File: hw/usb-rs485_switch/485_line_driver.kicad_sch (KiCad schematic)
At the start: 26 parts, among them Q15 Q_NPN_BEC, Q16 Si2301CDS, U26 INA180A2, U27 MAX485E

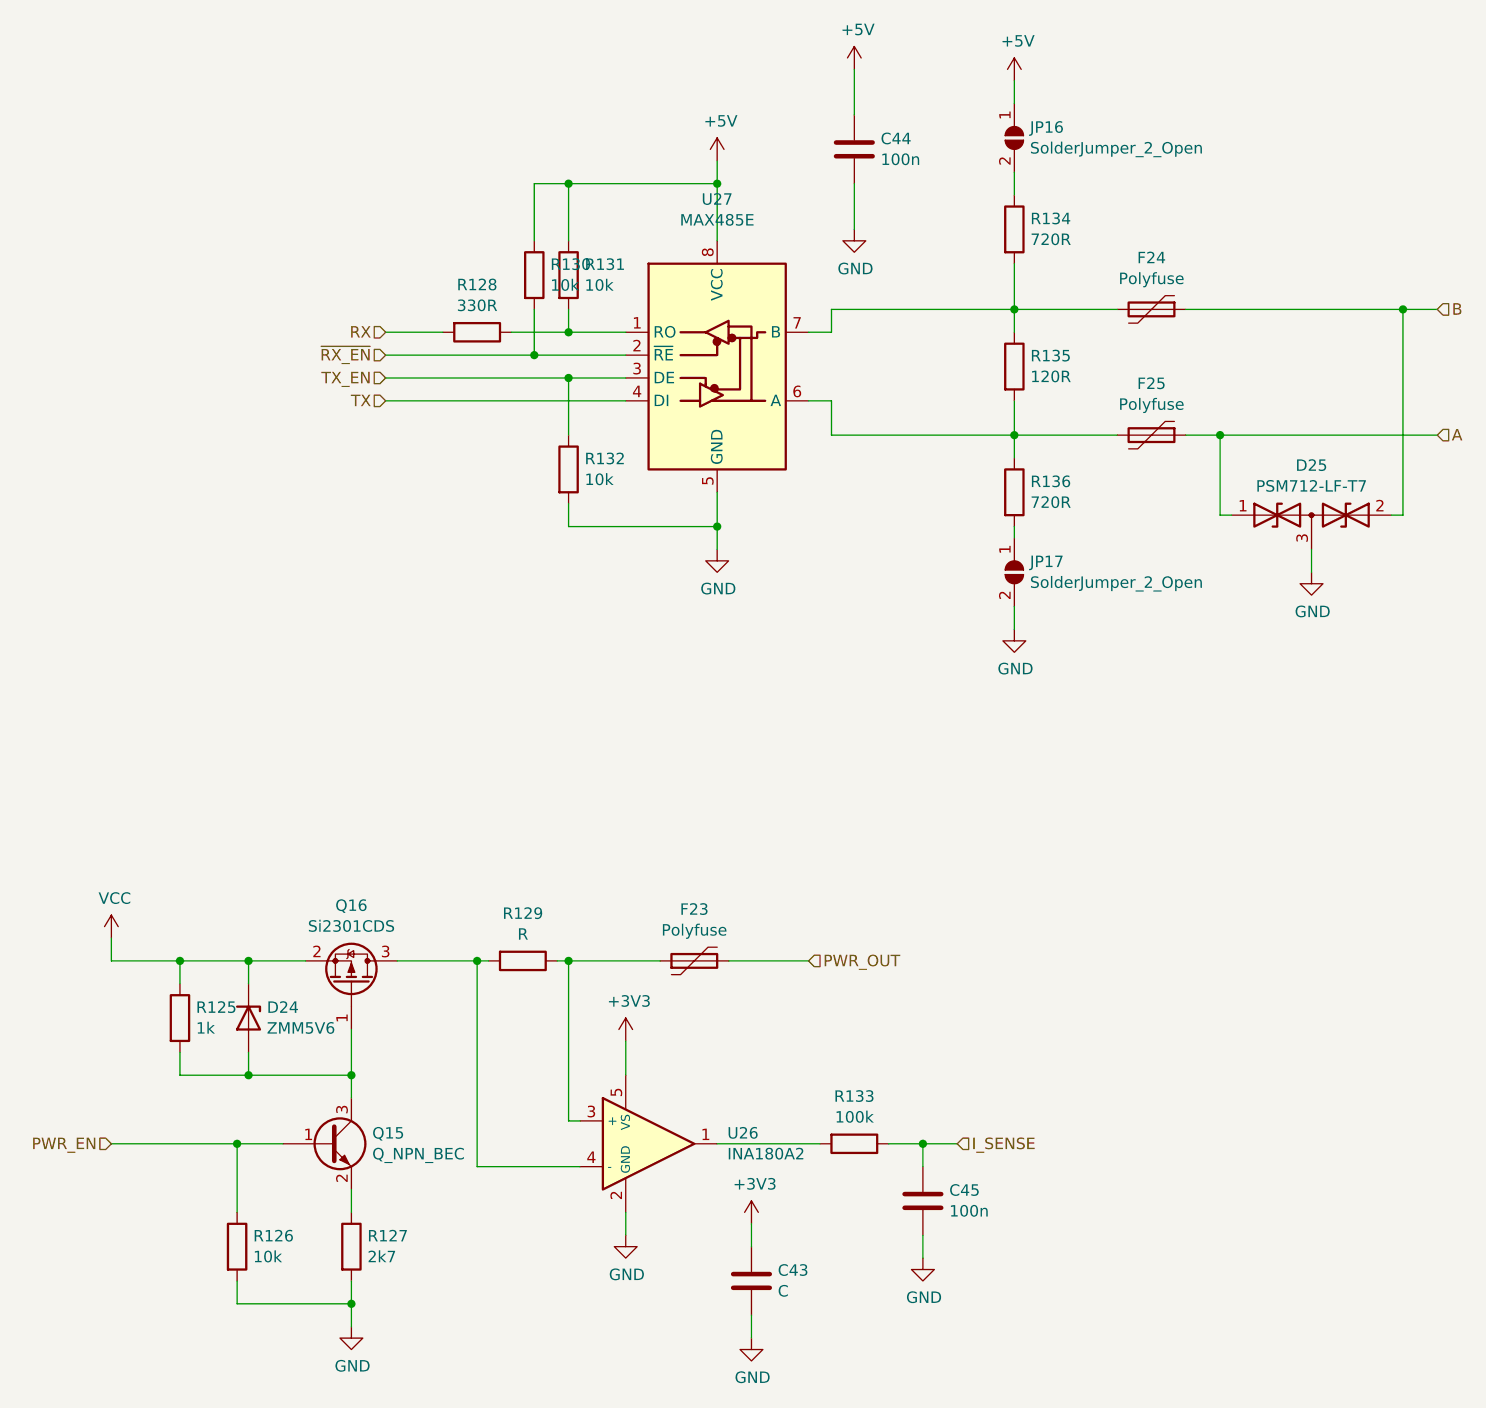
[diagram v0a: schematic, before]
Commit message: Assigned footprints, started routing.
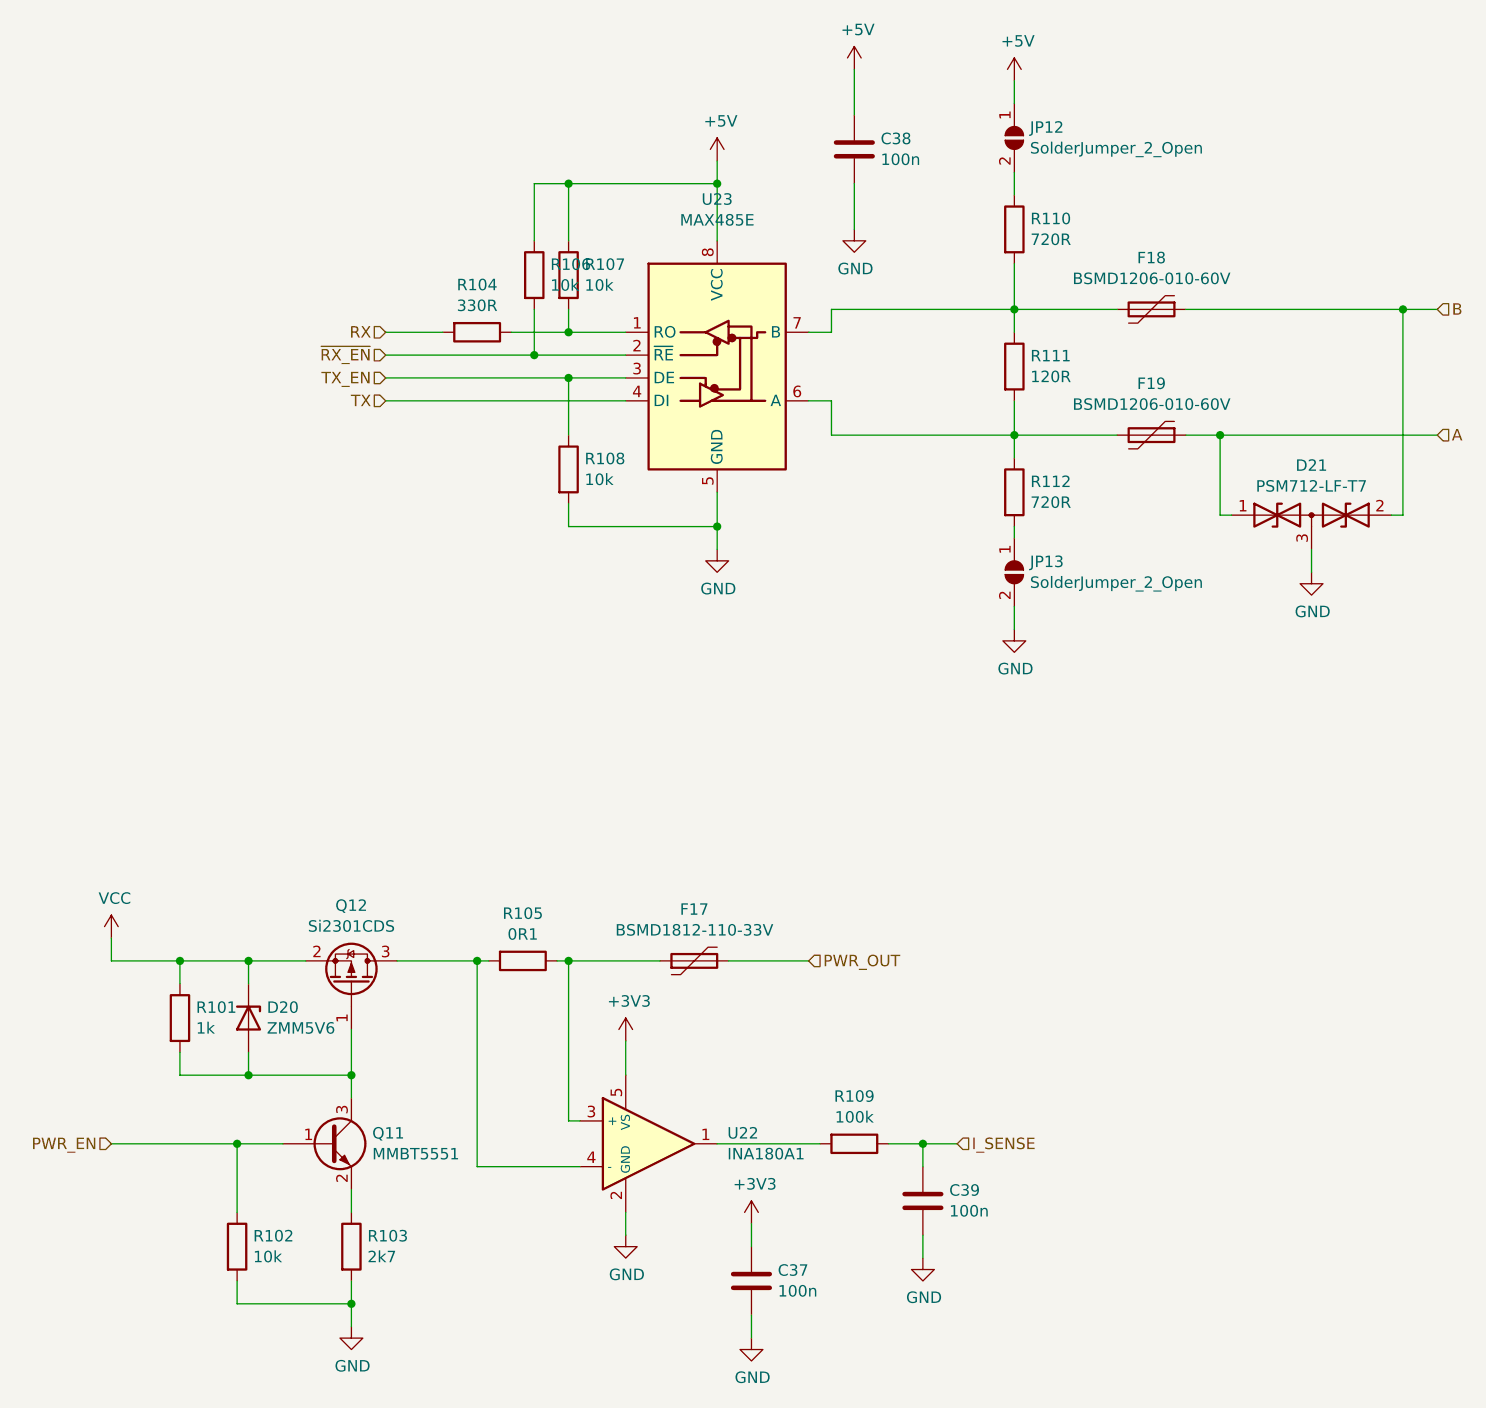
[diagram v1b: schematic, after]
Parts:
- C37: renamed from C43; value C -> 100n; footprint (none) -> Capacitor_SMD:C_0603_1608Metric
- C38: renamed from C44; footprint (none) -> Capacitor_SMD:C_0603_1608Metric
- C39: renamed from C45; footprint (none) -> Capacitor_SMD:C_0603_1608Metric
- D21: renamed from D25; footprint (none) -> Package_TO_SOT_SMD:SOT-23
- F17: renamed from F23; value Polyfuse -> BSMD1812-110-33V; footprint (none) -> Fuse:Fuse_1812_4532Metric; LCSC (none) -> C883150
- F18: renamed from F24; value Polyfuse -> BSMD1206-010-60V; footprint (none) -> Fuse:Fuse_1206_3216Metric; LCSC (none) -> C883116
- F19: renamed from F25; value Polyfuse -> BSMD1206-010-60V; footprint (none) -> Fuse:Fuse_1206_3216Metric; LCSC (none) -> C883116
- JP12: renamed from JP16; footprint (none) -> Jumper:SolderJumper-2_P1.3mm_Open_TrianglePad1.0x1.5mm
- JP13: renamed from JP17; footprint (none) -> Jumper:SolderJumper-2_P1.3mm_Open_TrianglePad1.0x1.5mm
- Q11: renamed from Q15; value Q_NPN_BEC -> MMBT5551; footprint (none) -> Package_TO_SOT_SMD:SOT-23; LCSC (none) -> C2145
- R101: renamed from R125; footprint (none) -> Resistor_SMD:R_0603_1608Metric
- R102: renamed from R126; footprint (none) -> Resistor_SMD:R_0603_1608Metric
- R103: renamed from R127; footprint (none) -> Resistor_SMD:R_0603_1608Metric
- R104: renamed from R128; footprint (none) -> Resistor_SMD:R_0603_1608Metric
- R105: renamed from R129; value R -> 0R1; footprint (none) -> Resistor_SMD:R_1206_3216Metric; LCSC (none) -> C25334
- R106: renamed from R130; footprint (none) -> Resistor_SMD:R_0603_1608Metric
- R107: renamed from R131; footprint (none) -> Resistor_SMD:R_0603_1608Metric
- R108: renamed from R132; footprint (none) -> Resistor_SMD:R_0603_1608Metric
- R109: renamed from R133; footprint (none) -> Resistor_SMD:R_0603_1608Metric
- R110: renamed from R134; footprint (none) -> Resistor_SMD:R_0603_1608Metric
- R111: renamed from R135; footprint (none) -> Resistor_SMD:R_0603_1608Metric
- R112: renamed from R136; footprint (none) -> Resistor_SMD:R_0603_1608Metric
- U22: renamed from U26; value INA180A2 -> INA180A1; footprint (none) -> Package_TO_SOT_SMD:SOT-23-5; LCSC (none) -> C122228
- U23: renamed from U27; footprint (none) -> Package_SO:SOIC-8_3.9x4.9mm_P1.27mm
- renumbered D24 to D20, Q16 to Q12

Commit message: Routing in progress.
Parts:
- renumbered C37 to C31, C38 to C32, C39 to C33, D20 to D16, D21 to D17, F17 to F11, F18 to F12, F19 to F13, JP12 to JP8, JP13 to JP9, Q11 to Q7, Q12 to Q8, R101 to R77, R102 to R78, R103 to R79, R104 to R80, R105 to R81, R106 to R82, R107 to R83, R108 to R84, R109 to R85, R110 to R86, R111 to R87, R112 to R88, U22 to U18, U23 to U19

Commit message: Routing in progress...
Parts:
- renumbered C31 to C25, C32 to C26, C33 to C27, D16 to D12, D17 to D13, F11 to F5, F12 to F6, F13 to F7, JP8 to JP4, JP9 to JP5, Q7 to Q3, Q8 to Q4, R77 to R53, R78 to R54, R79 to R55, R80 to R56, R81 to R57, R82 to R58, R83 to R59, R84 to R60, R85 to R61, R86 to R62, R87 to R63, R88 to R64, U18 to U14, U19 to U15

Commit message: Routed.
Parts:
- renumbered C25 to C22, C26 to C23, C27 to C24, D12 to D10, D13 to D11, F5 to F2, F6 to F3, F7 to F4, JP4 to JP2, JP5 to JP3, Q3 to Q1, Q4 to Q2, R53 to R41, R54 to R42, R55 to R43, R56 to R44, R57 to R45, R58 to R46, R59 to R47, R60 to R48, R61 to R49, R62 to R50, R63 to R51, R64 to R52, U14 to U12, U15 to U13
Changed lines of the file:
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@@
   (symbol (lib_id "Interface_UART:MAX485E") (at 118.11 67.31 0)
     (in_bom yes) (on_board yes)
-    (property "Reference" "U15" (id 0) (at 118.11 50.0126 0))
+    (property "Reference" "U13" (id 0) (at 118.11 50.0126 0))
     (property "Value" "MAX485E" (id 1) (at 118.11 52.324 0))
     (property "Footprint" "Package_SO:SOIC-8_3.9x4.9mm_P1.27mm" (id 2) (at 118.11 85.09 0)
@@
   (symbol (lib_id "Device:R") (at 151.13 53.34 0)
     (in_bom yes) (on_board yes)
-    (property "Reference" "R62" (id 0) (at 152.908 52.1716 0)
+    (property "Reference" "R50" (id 0) (at 152.908 52.1716 0)
       (effects (font (size 1.27 1.27)) (justify left))
     )
@@
   (symbol (lib_id "Device:R") (at 151.13 68.58 0)
     (in_bom yes) (on_board yes)
-    (property "Reference" "R63" (id 0) (at 152.908 67.4116 0)
+    (property "Reference" "R51" (id 0) (at 152.908 67.4116 0)
       (effects (font (size 1.27 1.27)) (justify left))
     )
@@
   (symbol (lib_id "Device:R") (at 151.13 82.55 0)
     (in_bom yes) (on_board yes)
-    (property "Reference" "R64" (id 0) (at 152.908 81.3816 0)
+    (property "Reference" "R52" (id 0) (at 152.908 81.3816 0)
       (effects (font (size 1.27 1.27)) (justify left))
     )
@@
   (symbol (lib_id "Device:Polyfuse") (at 166.37 62.23 270)
     (in_bom yes) (on_board yes)
-    (property "Reference" "F6" (id 0) (at 166.37 56.515 90))
+    (property "Reference" "F3" (id 0) (at 166.37 56.515 90))
     (property "Value" "BSMD1206-010-60V" (id 1) (at 166.37 58.8264 90))
     (property "Footprint" "Fuse:Fuse_1206_3216Metric" (id 2) (at 161.29 63.5 0)
@@
   (symbol (lib_id "Device:Polyfuse") (at 166.37 76.2 270)
     (in_bom yes) (on_board yes)
-    (property "Reference" "F7" (id 0) (at 166.37 70.485 90))
+    (property "Reference" "F4" (id 0) (at 166.37 70.485 90))
     (property "Value" "BSMD1206-010-60V" (id 1) (at 166.37 72.7964 90))
     (property "Footprint" "Fuse:Fuse_1206_3216Metric" (id 2) (at 161.29 77.47 0)
@@
   (symbol (lib_id "Device:C") (at 133.35 44.45 0)
     (in_bom yes) (on_board yes)
-    (property "Reference" "C26" (id 0) (at 136.271 43.2816 0)
+    (property "Reference" "C23" (id 0) (at 136.271 43.2816 0)
       (effects (font (size 1.27 1.27)) (justify left))
     )
@@
   (symbol (lib_id "Device:R") (at 101.6 58.42 0)
     (in_bom yes) (on_board yes)
-    (property "Reference" "R59" (id 0) (at 103.378 57.2516 0)
+    (property "Reference" "R47" (id 0) (at 103.378 57.2516 0)
       (effects (font (size 1.27 1.27)) (justify left))
     )
@@
   (symbol (lib_id "Device:R") (at 91.44 64.77 270)
     (in_bom yes) (on_board yes)
-    (property "Reference" "R56" (id 0) (at 91.44 59.5122 90))
+    (property "Reference" "R44" (id 0) (at 91.44 59.5122 90))
     (property "Value" "330R" (id 1) (at 91.44 61.8236 90))
     (property "Footprint" "Resistor_SMD:R_0603_1608Metric" (id 2) (at 91.44 62.992 90)
@@
   (symbol (lib_id "Device:D_TVS_x2_AAC") (at 184.15 85.09 0)
     (in_bom yes) (on_board yes)
-    (property "Reference" "D13" (id 0) (at 184.15 79.5782 0))
+    (property "Reference" "D11" (id 0) (at 184.15 79.5782 0))
     (property "Value" "PSM712-LF-T7" (id 1) (at 184.15 81.8896 0))
     (property "Footprint" "Package_TO_SOT_SMD:SOT-23" (id 2) (at 180.34 85.09 0)
@@
   (symbol (lib_id "Arm_interface_board-cache:custom_INA180") (at 110.49 154.94 0)
     (in_bom yes) (on_board yes)
-    (property "Reference" "U14" (id 0) (at 119.2276 153.7716 0)
+    (property "Reference" "U12" (id 0) (at 119.2276 153.7716 0)
       (effects (font (size 1.27 1.27)) (justify left))
     )
@@
   (symbol (lib_id "Device:R") (at 96.52 134.62 270)
     (in_bom yes) (on_board yes)
-    (property "Reference" "R57" (id 0) (at 96.52 129.3622 90))
+    (property "Reference" "R45" (id 0) (at 96.52 129.3622 90))
     (property "Value" "0R1" (id 1) (at 96.52 131.6736 90))
     (property "Footprint" "Resistor_SMD:R_1206_3216Metric" (id 2) (at 96.52 132.842 90)
@@
   (symbol (lib_id "Device:Polyfuse") (at 115.57 134.62 90)
     (in_bom yes) (on_board yes)
-    (property "Reference" "F5" (id 0) (at 115.57 128.905 90))
+    (property "Reference" "F2" (id 0) (at 115.57 128.905 90))
     (property "Value" "BSMD1812-110-33V" (id 1) (at 115.57 131.2164 90))
     (property "Footprint" "Fuse:Fuse_1812_4532Metric" (id 2) (at 120.65 133.35 0)
@@
   (symbol (lib_id "Transistor_FET:Si2319CDS") (at 77.47 137.16 270) (mirror x)
     (in_bom yes) (on_board yes)
-    (property "Reference" "Q4" (id 0) (at 77.47 128.4732 90))
+    (property "Reference" "Q2" (id 0) (at 77.47 128.4732 90))
     (property "Value" "Si2301CDS" (id 1) (at 77.47 130.7846 90))
     (property "Footprint" "Package_TO_SOT_SMD:SOT-23" (id 2) (at 75.565 132.08 0)
@@
   (symbol (lib_id "Device:R") (at 58.42 140.97 0)
     (in_bom yes) (on_board yes)
-    (property "Reference" "R53" (id 0) (at 60.198 139.8016 0)
+    (property "Reference" "R41" (id 0) (at 60.198 139.8016 0)
       (effects (font (size 1.27 1.27)) (justify left))
     )
@@
   (symbol (lib_id "Diode:ZMMxx") (at 66.04 140.97 270)
     (in_bom yes) (on_board yes)
-    (property "Reference" "D12" (id 0) (at 68.072 139.8016 90)
+    (property "Reference" "D10" (id 0) (at 68.072 139.8016 90)
       (effects (font (size 1.27 1.27)) (justify left))
     )
@@
   (symbol (lib_id "Device:Q_NPN_BEC") (at 74.93 154.94 0)
     (in_bom yes) (on_board yes)
-    (property "Reference" "Q3" (id 0) (at 79.7814 153.7716 0)
+    (property "Reference" "Q1" (id 0) (at 79.7814 153.7716 0)
       (effects (font (size 1.27 1.27)) (justify left))
     )
@@
   (symbol (lib_id "Device:R") (at 77.47 166.37 0)
     (in_bom yes) (on_board yes)
-    (property "Reference" "R55" (id 0) (at 79.248 165.2016 0)
+    (property "Reference" "R43" (id 0) (at 79.248 165.2016 0)
       (effects (font (size 1.27 1.27)) (justify left))
     )
@@
   (symbol (lib_id "Device:C") (at 121.92 170.18 0)
     (in_bom yes) (on_board yes)
-    (property "Reference" "C25" (id 0) (at 124.841 169.0116 0)
+    (property "Reference" "C22" (id 0) (at 124.841 169.0116 0)
       (effects (font (size 1.27 1.27)) (justify left))
     )
@@
   (symbol (lib_id "Device:R") (at 97.79 58.42 0)
     (in_bom yes) (on_board yes)
-    (property "Reference" "R58" (id 0) (at 99.568 57.2516 0)
+    (property "Reference" "R46" (id 0) (at 99.568 57.2516 0)
       (effects (font (size 1.27 1.27)) (justify left))
     )
@@
   (symbol (lib_id "Device:R") (at 101.6 80.01 0)
     (in_bom yes) (on_board yes)
-    (property "Reference" "R60" (id 0) (at 103.378 78.8416 0)
+    (property "Reference" "R48" (id 0) (at 103.378 78.8416 0)
       (effects (font (size 1.27 1.27)) (justify left))
     )
@@
   (symbol (lib_id "Device:R") (at 64.77 166.37 0)
     (in_bom yes) (on_board yes)
-    (property "Reference" "R54" (id 0) (at 66.548 165.2016 0)
+    (property "Reference" "R42" (id 0) (at 66.548 165.2016 0)
       (effects (font (size 1.27 1.27)) (justify left))
     )
@@
   (symbol (lib_id "Jumper:SolderJumper_2_Open") (at 151.13 91.44 270)
     (in_bom yes) (on_board yes)
-    (property "Reference" "JP5" (id 0) (at 152.8572 90.2716 90)
+    (property "Reference" "JP3" (id 0) (at 152.8572 90.2716 90)
       (effects (font (size 1.27 1.27)) (justify left))
     )
@@
   (symbol (lib_id "Jumper:SolderJumper_2_Open") (at 151.13 43.18 270)
     (in_bom yes) (on_board yes)
-    (property "Reference" "JP4" (id 0) (at 152.8572 42.0116 90)
+    (property "Reference" "JP2" (id 0) (at 152.8572 42.0116 90)
       (effects (font (size 1.27 1.27)) (justify left))
     )
@@
   (symbol (lib_id "Device:R") (at 133.35 154.94 270)
     (in_bom yes) (on_board yes)
-    (property "Reference" "R61" (id 0) (at 133.35 149.6822 90))
+    (property "Reference" "R49" (id 0) (at 133.35 149.6822 90))
     (property "Value" "100k" (id 1) (at 133.35 151.9936 90))
     (property "Footprint" "Resistor_SMD:R_0603_1608Metric" (id 2) (at 133.35 153.162 90)
@@
   (symbol (lib_id "Device:C") (at 140.97 161.29 0)
     (in_bom yes) (on_board yes)
-    (property "Reference" "C27" (id 0) (at 143.891 160.1216 0)
-      (effects (font (size 1.27 1.27)) (justify left))
-    )
+    (property "Reference" "C24" (id 0) (at 143.891 160.1216 0)
+      (effects (font (size 1.27 1.27)) (justify left))
+    )
